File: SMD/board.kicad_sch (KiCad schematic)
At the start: 28 parts, among them J1 9V Battery, J2 Barrel_Jack_Switch, J3 USB_B, J4 1, J5 2, J6 Conn_02x04_Odd_Even, SW1 SW_DIP_x04, U1 LM317_3PinPackage, U2 AMS1117-5.0, U3 AMS1117-3.3

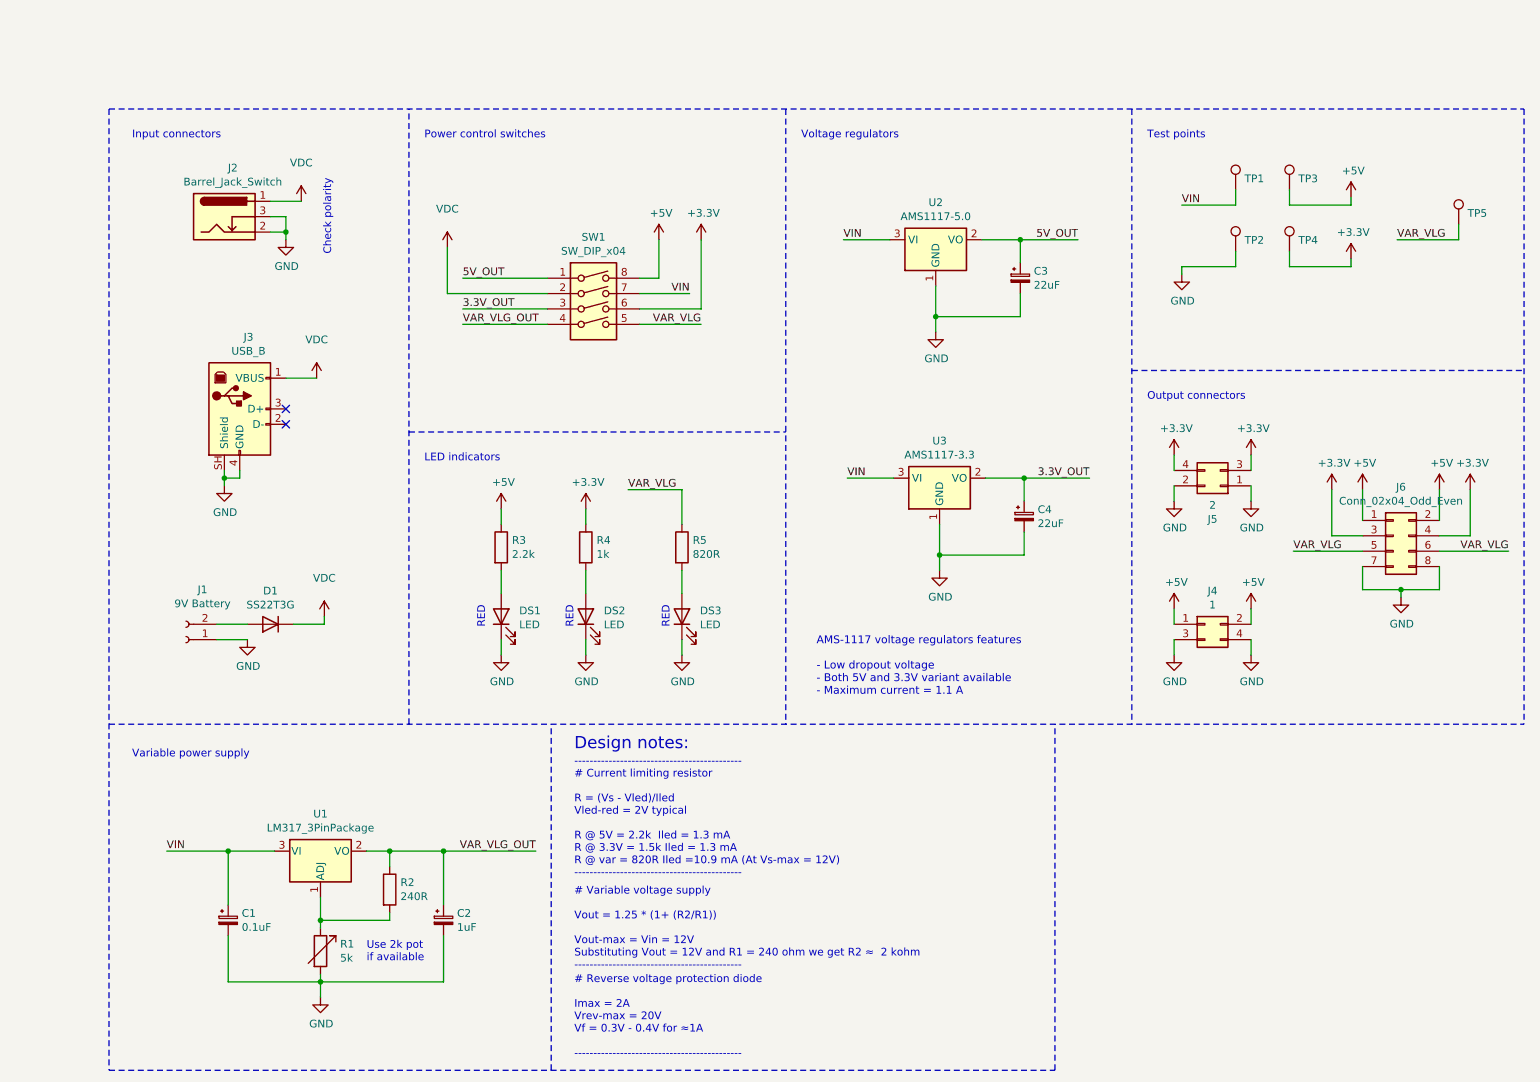
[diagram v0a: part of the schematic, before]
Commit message: SMD Kicad 10
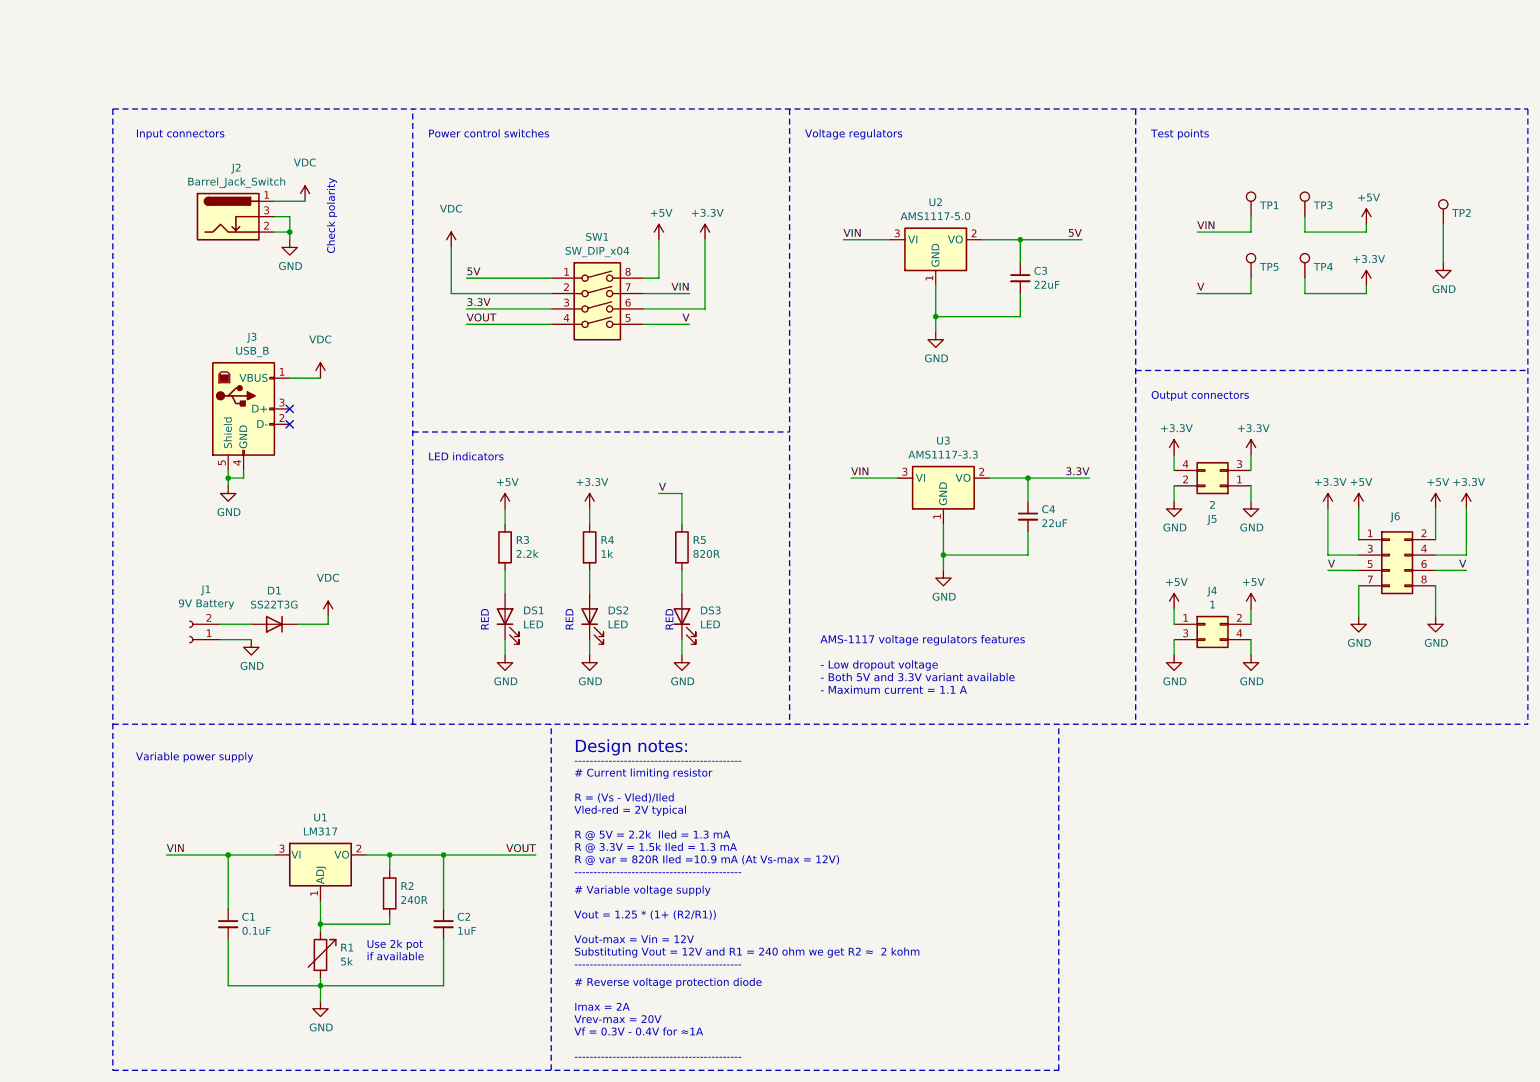
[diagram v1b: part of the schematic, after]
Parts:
- C1, C2, C3, C4: footprint Capacitor_SMD:C_1206_3216Metric_Pad1.42x1.75mm_HandSolder -> Capacitor_SMD:C_1206_3216Metric_Pad1.33x1.80mm_HandSolder; symbol Device:CP_Small -> Device:C_Small
- J1: symbol Connector:Conn_01x02_Female -> Connector:Conn_01x02_Socket
- J2: footprint Breadboard_Power_Supply:BarrelJack_CUI_PJ-102AH_Horizontal -> Board:BarrelJack_CUI_PJ-102AH_Horizontal
- J3: footprint Breadboard_Power_Supply:USB_B_OST_USB-B1HSxx_Horizontal -> Board:USB_B_OST_USB-B1HSxx_Horizontal; symbol Connector:USB_B -> Board:USB_B
- R2, R3, R4, R5: footprint Resistor_SMD:R_0805_2012Metric_Pad1.15x1.40mm_HandSolder -> Resistor_SMD:R_0805_2012Metric_Pad1.20x1.40mm_HandSolder
- U1: value LM317_3PinPackage -> LM317; footprint Package_TO_SOT_SMD:SOT-223 -> Package_TO_SOT_SMD:SOT-223-3_TabPin2; symbol Regulator_Linear:LM317_3PinPackage -> Regulator_Linear:LM317_SOT-223
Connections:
- net GND: now also J3.5 (Shield); no longer J3.SH (Shield)
- net 3.3V_OUT renamed 3.3V
- net 5V_OUT renamed 5V
- net VAR_VLG renamed V
- net VAR_VLG_OUT renamed VOUT
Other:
- moved on the sheet: D1, DS1, DS2, J1, J2, J3, J6, R1, R2, R3, R4, SW1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
